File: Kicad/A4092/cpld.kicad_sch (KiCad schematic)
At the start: 15 parts, among them J2 Conn_01x06_Pin, U7 AMS1117-3.3, U9 XC95144XL-TQ144

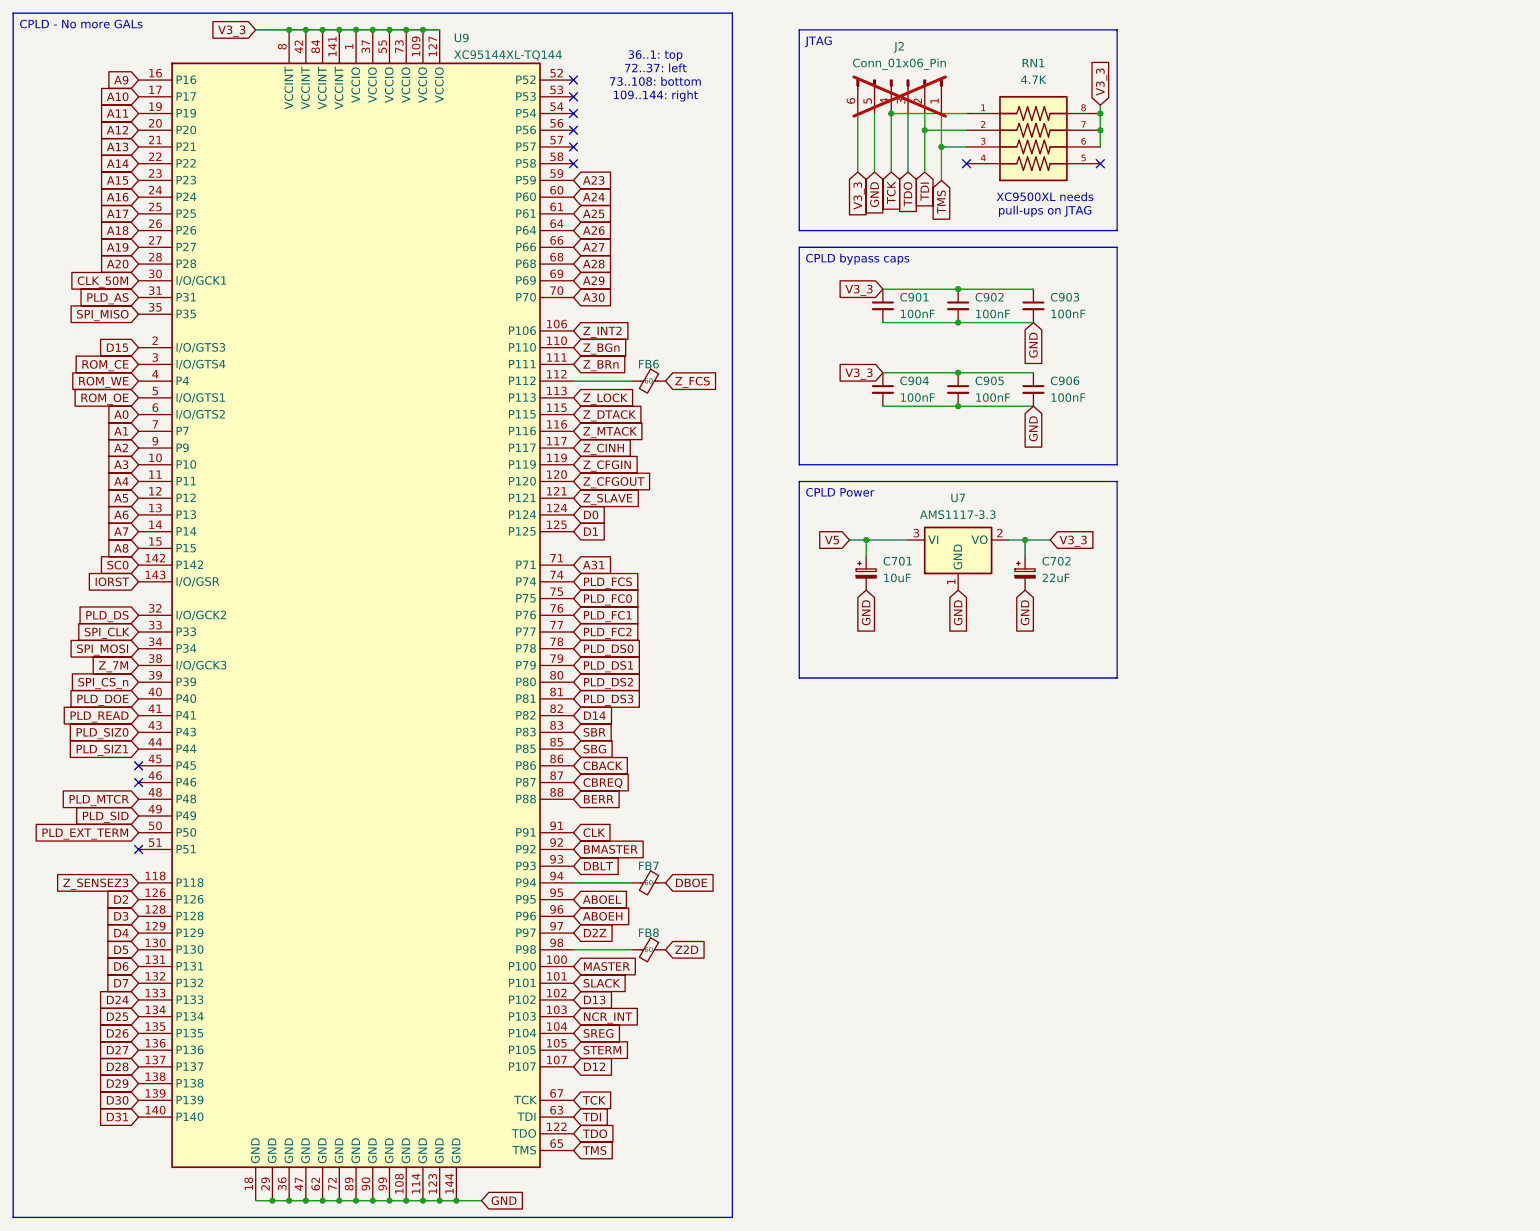
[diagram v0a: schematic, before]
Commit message: A4092 Schematics Revision C
- Power U5 / 74LVC07 from 3.3V rail
- Use ABOEH for 1OEAB on U4 / 74ABT16543
- Add bypass capacitor C501 for U5 / 74LVC07
- Remove EMI filters and capacitors from SCSI lines. They
  are a net negative for signal integrity
- Remove DIP switch circuit as all options are controlled
  by the CPLD / AutoConfig ROM now.
- Remove parallel flash memory, as SPI works reliably and
  is significantly easier to source.
- Remove all ferrite beads from signal lines, as these were
  populated with 0 Ohm resistors in all Proto devices.
- Mark power connector and 12V capacitor as DNP
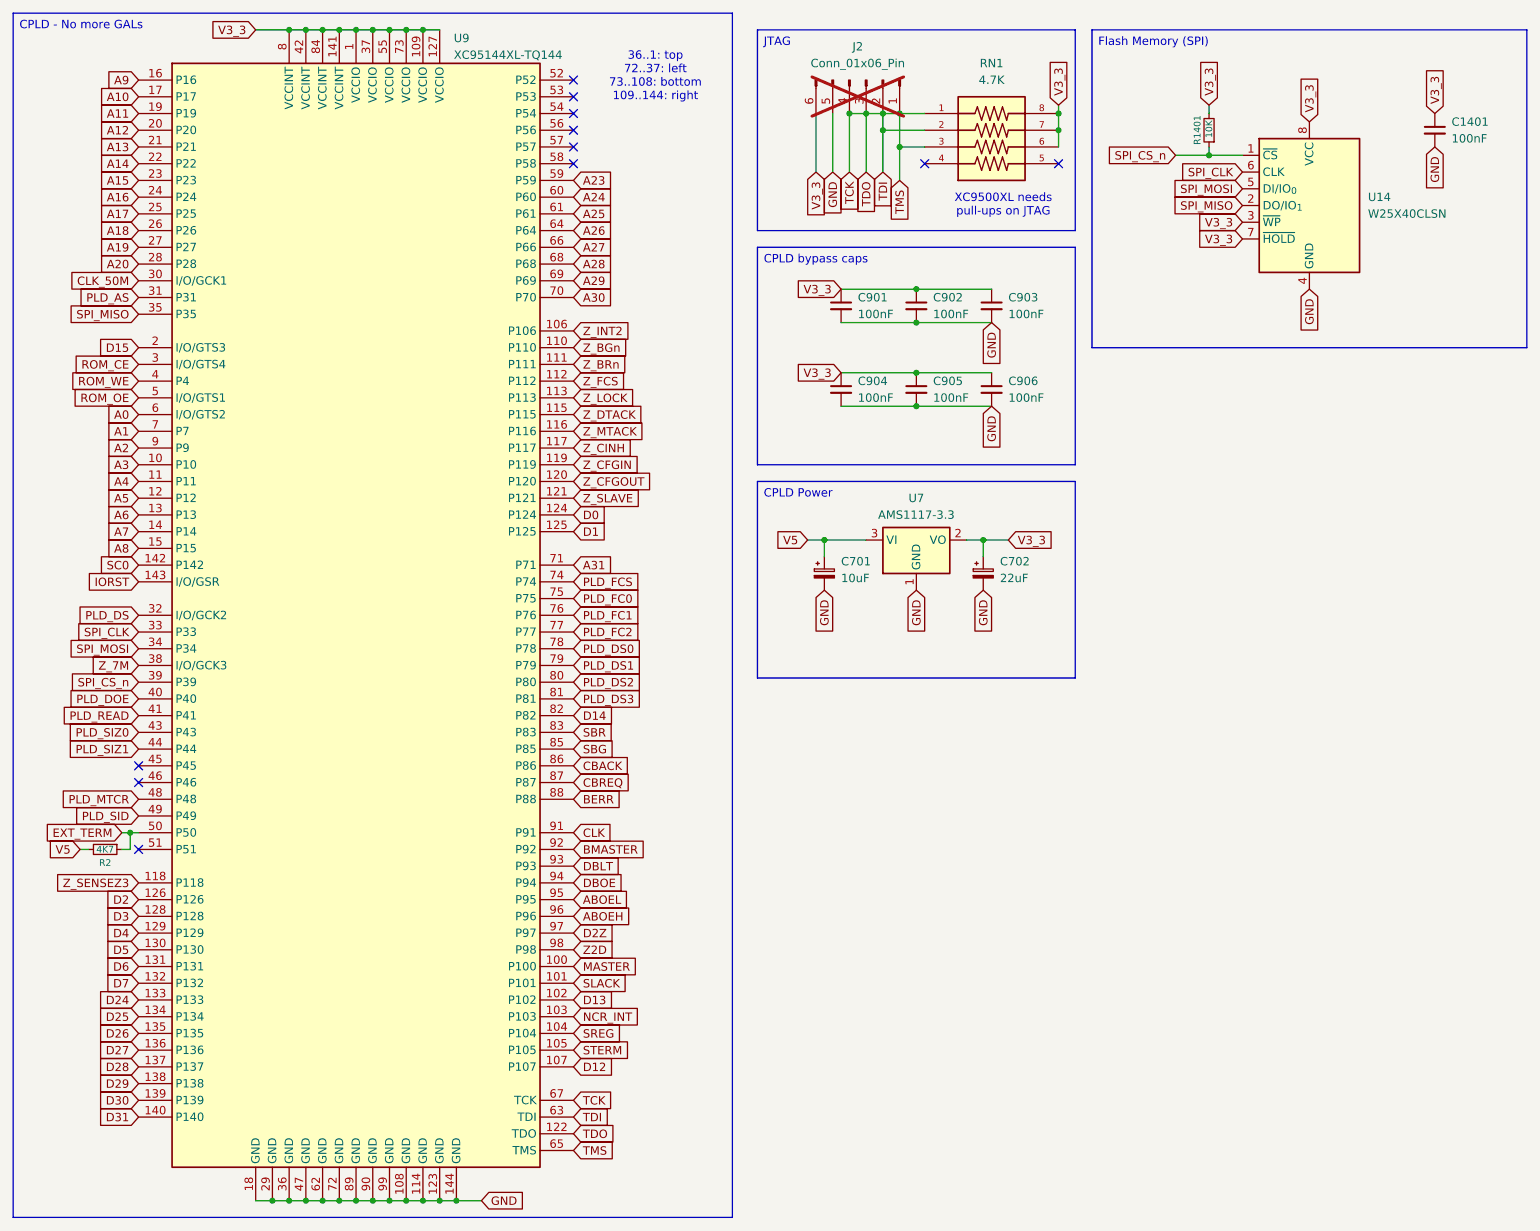
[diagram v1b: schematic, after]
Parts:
- removed FB6, FB7, FB8: 60, Capacitor_SMD:C_0603_1608Metric_Pad1.08x0.95mm_HandSolder, symbol Device:FerriteBead_Small
- added C1401: 100nF, Capacitor_SMD:C_0603_1608Metric_Pad1.08x0.95mm_HandSolder, symbol Device:C_Small
- added R1401: 10K, Resistor_SMD:R_0603_1608Metric_Pad0.98x0.95mm_HandSolder, symbol Device:R_Small
- added R2: 4K7, Resistor_SMD:R_0603_1608Metric_Pad0.98x0.95mm_HandSolder, symbol Device:R_Small
- added U14: W25X40CLSN, Package_SO:SOIC-8_3.9x4.9mm_P1.27mm, symbol Memory_Flash:W25X40CLSN
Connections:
- net TDI is gone; now on net TCK: J2.2 (Pin_2), RN1.2, U9.63 (TDI)
- net TDO is gone; now on net TCK: J2.3 (Pin_3), U9.122 (TDO)
- net TMS is gone; now on net TCK: J2.1 (Pin_1), RN1.3, U9.65 (TMS)
- net DBOE: now also U9.94 (P94)
- net GND: now also C1401.2, U14.4 (GND)
- net SPI_CLK: now also U14.6 (CLK)
- net SPI_CS_n: now also R1401.1, U14.1 (~{CS})
- net SPI_MISO: now also U14.2 (DO/IO_{1})
- net SPI_MOSI: now also U14.5 (DI/IO_{0})
- net V3_3: now also C1401.1, R1401.2, U14.3 (~{WP}), U14.7 (~{HOLD}), U14.8 (VCC)
- net V5: now also R2.2
- net Z2D: now also U9.98 (P98)
- net Z_FCS: now also U9.112 (P112)
- net PLD_EXT_TERM renamed EXT_TERM
- net EXT_TERM: now also R2.1
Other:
- moved on the sheet: C701, C702, C901, C902, C903, C904, C905, C906, J2, RN1, U7
